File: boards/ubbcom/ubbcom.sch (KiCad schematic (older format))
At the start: 23 parts, among them U1 FT232RL

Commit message: blah, quick update... btw, this layout is horrible -- just testing to see if I can make this work
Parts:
- C1, C2, C3, R1, R2, R3: footprint (none) -> SM0805
- C4, FB1: footprint (none) -> SM0603
- D1, D2, D3: footprint (none) -> LED-1206
- PCTS1, PDCD1, PDCR1, PDTR1, PGND1, PRI1, PRTS1, PRXD1, PTXD1, PVCC1: footprint (none) -> SIL-1
- PUSB1: footprint (none) -> SIL-4
- U1: footprint (none) -> SSOP28
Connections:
- net GND: now also PUSB1.4 (P4); no longer PUSB1.1 (P1)
- net at PUSB1.2 (P2): now also U1.16 (USBD-); no longer U1.15 (USBD+)
- net at PUSB1.3 (P3): now also U1.15 (USBD+); no longer U1.16 (USBD-)
- net at C1.1, FB1.1: now also PUSB1.1 (P1); no longer PUSB1.4 (P4)
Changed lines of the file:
@@
-EESchema Schematic File Version 2  date Sun 13 May 2012 06:31:02 AM EDT
+EESchema Schematic File Version 2  date Sun 13 May 2012 07:41:58 AM EDT
 LIBS:power
 LIBS:device
@@
 F 0 "PUSB1" V 2000 2350 50  0000 C CNN
 F 1 "CONN_4" V 2100 2350 50  0000 C CNN
+F 2 "SIL-4" V 2200 2350 50  0001 C CNN
 	1    2050 2350
-	-1   0    0    1
+	-1   0    0    -1
 $EndComp
 $Comp
@@
 F 0 "FB1" H 2850 2350 60  0000 C CNN
 F 1 "FILTER" H 3100 2350 60  0000 C CNN
+F 2 "SM0603" H 3100 2450 60  0001 C CNN
 	1    3000 2200
 	1    0    0    -1
@@
 F 0 "C1" H 2600 2850 50  0000 L CNN
 F 1 "10nF" H 2600 2650 50  0000 L CNN
+F 2 "SM0805" H 2600 2750 50  0001 C CNN
 	1    2550 2750
 	1    0    0    -1
@@
 F 0 "C2" H 3500 2850 50  0000 L CNN
 F 1 "0.1uF" H 3350 2650 50  0000 L CNN
+F 2 "SM0805" H 3350 2750 50  0001 C CNN
 	1    3450 2750
 	1    0    0    -1
@@
 F 0 "C3" H 3800 2850 50  0000 L CNN
 F 1 "4.7uF" H 3650 2650 50  0000 L CNN
+F 2 "SM0805" H 3650 2750 50  0001 C CNN
 	1    3750 2750
 	1    0    0    -1
@@
 F 0 "D1" H 7000 3400 50  0000 C CNN
 F 1 "LED" H 7000 3200 50  0000 C CNN
+F 2 "LED-1206" H 7000 3300 50  0001 C CNN
 	1    7000 3300
 	0    -1   -1   0
@@
 F 0 "R1" V 7080 3800 50  0000 C CNN
 F 1 "1K" V 7000 3800 50  0000 C CNN
+F 2 "SM0805" V 7100 3800 50  0001 C CNN
 	1    7000 3800
 	1    0    0    -1
@@
 F 0 "U1" H 5250 3700 60  0000 C CNN
 F 1 "FT232RL" H 5650 1800 60  0000 L CNN
+F 2 "SSOP28" H 5650 1900 60  0001 C CNN
 	1    5250 2800
 	1    0    0    -1
@@
 F 0 "D2" H 6400 3400 50  0000 C CNN
 F 1 "LED" H 6400 3200 50  0000 C CNN
+F 2 "LED-1206" H 6400 3300 50  0001 C CNN
 	1    6400 3300
 	0    -1   -1   0
@@
 F 0 "D3" H 6700 3400 50  0000 C CNN
 F 1 "LED" H 6700 3200 50  0000 C CNN
+F 2 "LED-1206" H 6700 3300 50  0001 C CNN
 	1    6700 3300
 	0    -1   -1   0
@@
 F 0 "R3" V 6480 3800 50  0000 C CNN
 F 1 "1K" V 6400 3800 50  0000 C CNN
+F 2 "SM0805" V 6500 3800 50  0001 C CNN
 	1    6400 3800
 	1    0    0    -1
@@
 F 0 "R2" V 6780 3800 50  0000 C CNN
 F 1 "1K" V 6700 3800 50  0000 C CNN
+F 2 "SM0805" V 6800 3800 50  0001 C CNN
 	1    6700 3800
 	1    0    0    -1
@@
 F 0 "C4" H 4200 3600 50  0000 L CNN
 F 1 "0.1uF" H 4050 3400 50  0000 L CNN
+F 2 "SM0603" H 4050 3500 50  0001 C CNN
 	1    4150 3500
 	1    0    0    -1
@@
 F 0 "PTXD1" H 6630 2100 40  0000 L CNN
 F 1 "CONN_1" H 6550 2155 30  0001 C CNN
+F 2 "SIL-1" H 6550 2255 30  0001 C CNN
 	1    6550 2100
 	1    0    0    -1
@@
 F 0 "PRXD1" H 6630 2200 40  0000 L CNN
 F 1 "CONN_1" H 6550 2255 30  0001 C CNN
+F 2 "SIL-1" H 6550 2355 30  0001 C CNN
 	1    6550 2200
 	1    0    0    -1
@@
 F 0 "PRTS1" H 6630 2300 40  0000 L CNN
 F 1 "CONN_1" H 6550 2355 30  0001 C CNN
+F 2 "SIL-1" H 6550 2455 30  0001 C CNN
 	1    6550 2300
 	1    0    0    -1
@@
 F 0 "PCTS1" H 6630 2400 40  0000 L CNN
 F 1 "CONN_1" H 6550 2455 30  0001 C CNN
+F 2 "SIL-1" H 6550 2555 30  0001 C CNN
 	1    6550 2400
 	1    0    0    -1
@@
 F 0 "PDTR1" H 6630 2500 40  0000 L CNN
 F 1 "CONN_1" H 6550 2555 30  0001 C CNN
+F 2 "SIL-1" H 6550 2655 30  0001 C CNN
 	1    6550 2500
 	1    0    0    -1
@@
 F 0 "PDCR1" H 6630 2600 40  0000 L CNN
 F 1 "CONN_1" H 6550 2655 30  0001 C CNN
+F 2 "SIL-1" H 6550 2755 30  0001 C CNN
 	1    6550 2600
 	1    0    0    -1
@@
 F 0 "PDCD1" H 6630 2700 40  0000 L CNN
 F 1 "CONN_1" H 6550 2755 30  0001 C CNN
+F 2 "SIL-1" H 6550 2855 30  0001 C CNN
 	1    6550 2700
 	1    0    0    -1
@@
 F 0 "PRI1" H 6630 2800 40  0000 L CNN
 F 1 "CONN_1" H 6550 2855 30  0001 C CNN
+F 2 "SIL-1" H 6550 2955 30  0001 C CNN
 	1    6550 2800
 	1    0    0    -1
@@
 F 0 "PVCC1" H 7580 4050 40  0000 L CNN
 F 1 "CONN_1" H 7500 4105 30  0001 C CNN
+F 2 "SIL-1" H 7500 4205 30  0001 C CNN
 	1    7500 4050
 	1    0    0    -1
@@
 F 0 "PGND1" H 7580 3100 40  0000 L CNN
 F 1 "CONN_1" H 7500 3155 30  0001 C CNN
+F 2 "SIL-1" H 7500 3255 30  0001 C CNN
 	1    7500 3100
 	1    0    0    -1
 $EndComp
 Wire Wire Line
-	2400 2200 2550 2200
-Wire Wire Line
-	2550 2200 2650 2200
+	2400 2200 2650 2200
 Wire Wire Line
 	2400 2300 4300 2300
@@
 	4300 2150 4100 2150
 Wire Wire Line
-	4100 2050 4100 2150
-Wire Wire Line
-	4100 2150 4100 2200
+	4100 2050 4100 2200
 Connection ~ 4300 2150
 Wire Wire Line
-	4100 2200 3750 2200
-Wire Wire Line
-	3750 2200 3450 2200
-Wire Wire Line
-	3450 2200 3350 2200
+	4100 2200 3350 2200
 Connection ~ 4100 2150
 Wire Wire Line
@@
 	2400 2500 2400 2950
 Wire Wire Line
-	2400 2950 2550 2950
-Wire Wire Line
-	2550 2950 3000 2950
-Wire Wire Line
-	3000 2950 3450 2950
-Wire Wire Line
-	3450 2950 3750 2950
+	2400 2950 3750 2950
 Wire Wire Line
 	3450 2200 3450 2550
@@
 	6700 3500 6700 3550
 Wire Wire Line
-	6400 4050 6700 4050
-Wire Wire Line
-	6700 4050 7000 4050
-Wire Wire Line
-	7000 4050 7250 4050
-Wire Wire Line
-	7250 4050 7350 4050
+	6400 4050 7350 4050
 Wire Wire Line
 	7250 4050 7250 4000
@@
 	7000 3500 7000 3550
 Wire Wire Line
-	7000 3100 7250 3100
-Wire Wire Line
-	7250 3100 7350 3100
+	7000 3100 7350 3100
 Wire Wire Line
 	7250 3100 7250 3150
 Wire Wire Line
-	4950 4000 5100 4000
-Wire Wire Line
-	5100 4000 5250 4000
-Wire Wire Line
-	5250 4000 5400 4000
-Wire Wire Line
-	5400 4000 5550 4000
+	4950 4000 5550 4000
 Connection ~ 5100 4000
 Connection ~ 5100 4000

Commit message: yay done!
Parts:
- removed PDCD1, PDCR1, PRI1, PRTS1: CONN_1, SIL-1, symbol CONN_1
- added J1: USBPCB, SparkFun-USB-A-PCB, symbol USBPCB
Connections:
- net GND: now also J1.GND
- net at C1.1, FB1.1, PUSB1.1 (P1): now also J1.5V (VBUS)
- net at PUSB1.2 (P2), U1.16 (USBD-): now also J1.USBm (D-)
- net at PUSB1.3 (P3), U1.15 (USBD+): now also J1.USBp (D+)
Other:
- moved on the sheet: PUSB1
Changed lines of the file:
@@
-EESchema Schematic File Version 2  date Sun 13 May 2012 07:41:58 AM EDT
+EESchema Schematic File Version 2  date Tue 15 May 2012 01:46:11 AM EDT
 LIBS:power
 LIBS:device
@@
 LIBS:contrib
 LIBS:valves
-EELAYER 43  0
+LIBS:SparkFun
+LIBS:ubbcom-cache
+EELAYER 25  0
 EELAYER END
 $Descr A4 11693 8268
@@
 Sheet 1 1
 Title ""
-Date "13 may 2012"
+Date "15 may 2012"
 Rev ""
 Comp ""
@@
 L CONN_4 PUSB1
 U 1 1 4FAF7B95
-P 2050 2350
-F 0 "PUSB1" V 2000 2350 50  0000 C CNN
-F 1 "CONN_4" V 2100 2350 50  0000 C CNN
-F 2 "SIL-4" V 2200 2350 50  0001 C CNN
-	1    2050 2350
+P 1500 2350
+F 0 "PUSB1" V 1450 2350 50  0000 C CNN
+F 1 "CONN_4" V 1550 2350 50  0000 C CNN
+F 2 "SIL-4" V 1650 2350 50  0001 C CNN
+	1    1500 2350
 	-1   0    0    -1
 $EndComp
@@
 $EndComp
 $Comp
-L CONN_1 PRTS1
-U 1 1 4FAF87D2
-P 6550 2300
-F 0 "PRTS1" H 6630 2300 40  0000 L CNN
-F 1 "CONN_1" H 6550 2355 30  0001 C CNN
-F 2 "SIL-1" H 6550 2455 30  0001 C CNN
-	1    6550 2300
-	1    0    0    -1
-$EndComp
-$Comp
 L CONN_1 PCTS1
 U 1 1 4FAF87D9
@@
 $EndComp
 $Comp
-L CONN_1 PDCR1
-U 1 1 4FAF87E7
-P 6550 2600
-F 0 "PDCR1" H 6630 2600 40  0000 L CNN
-F 1 "CONN_1" H 6550 2655 30  0001 C CNN
-F 2 "SIL-1" H 6550 2755 30  0001 C CNN
-	1    6550 2600
-	1    0    0    -1
-$EndComp
-$Comp
-L CONN_1 PDCD1
-U 1 1 4FAF87EE
-P 6550 2700
-F 0 "PDCD1" H 6630 2700 40  0000 L CNN
-F 1 "CONN_1" H 6550 2755 30  0001 C CNN
-F 2 "SIL-1" H 6550 2855 30  0001 C CNN
-	1    6550 2700
-	1    0    0    -1
-$EndComp
-$Comp
-L CONN_1 PRI1
-U 1 1 4FAF87F5
-P 6550 2800
-F 0 "PRI1" H 6630 2800 40  0000 L CNN
-F 1 "CONN_1" H 6550 2855 30  0001 C CNN
-F 2 "SIL-1" H 6550 2955 30  0001 C CNN
-	1    6550 2800
-	1    0    0    -1
-$EndComp
-$Comp
 L CONN_1 PVCC1
 U 1 1 4FAF8880
@@
 	1    0    0    -1
 $EndComp
-Wire Wire Line
-	2400 2200 2650 2200
-Wire Wire Line
-	2400 2300 4300 2300
+$Comp
+L USBPCB J1
+U 1 1 4FB1EF10
+P 1950 2000
+F 0 "J1" H 2050 2400 50  0000 C CNN
+F 1 "USBPCB" H 2050 1900 50  0000 C CNN
+F 2 "SparkFun-USB-A-PCB" H 2050 1800 50  0001 C CNN
+	1    1950 2000
+	0    1    -1   0
+$EndComp
+Wire Wire Line
+	2650 2200 1850 2200
+Wire Wire Line
+	1850 2300 4300 2300
 Wire Wire Line
 	4300 2300 4300 2400
 Wire Wire Line
-	2400 2400 4200 2400
+	1850 2400 4200 2400
 Wire Wire Line
 	4200 2400 4200 2500
@@
 Connection ~ 2550 2200
 Wire Wire Line
-	2400 2500 2400 2950
+	2400 2950 2400 2500
 Wire Wire Line
 	2400 2950 3750 2950
@@
 Connection ~ 3000 2950
 Wire Wire Line
-	6150 2300 6400 2300
-Wire Wire Line
 	6150 2400 6400 2400
 Wire Wire Line
 	6150 2500 6400 2500
-Wire Wire Line
-	6150 2600 6400 2600
-Wire Wire Line
-	6150 2700 6400 2700
-Wire Wire Line
-	6150 2800 6400 2800
 Connection ~ 7250 4050
 Connection ~ 7250 4050
 Connection ~ 7250 3100
 Connection ~ 7250 3100
+Wire Wire Line
+	2050 2200 2050 2100
+Wire Wire Line
+	2150 2300 2150 2100
+Wire Wire Line
+	2250 2400 2250 2100
+Wire Wire Line
+	1950 2100 1950 2500
+Wire Wire Line
+	2400 2500 1850 2500
+Connection ~ 2050 2200
+Connection ~ 2150 2300
+Connection ~ 2250 2400
+Connection ~ 1950 2500
 $EndSCHEMATC

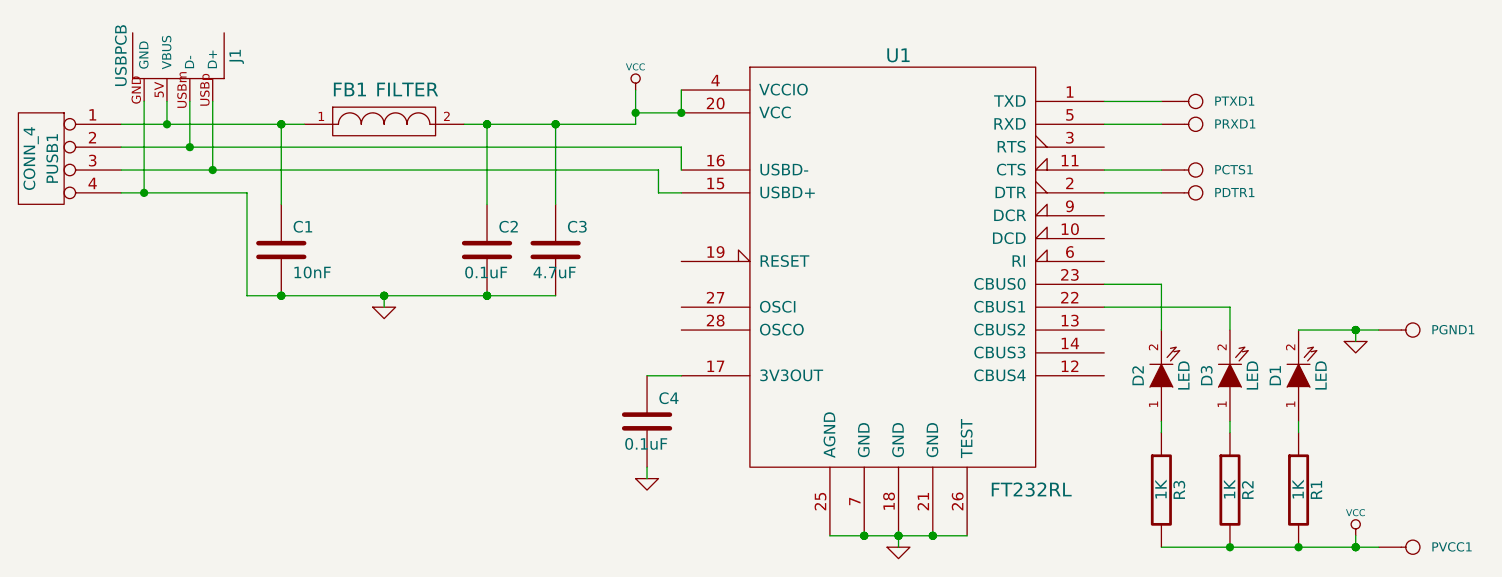
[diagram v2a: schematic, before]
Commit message: update to include txden and rts
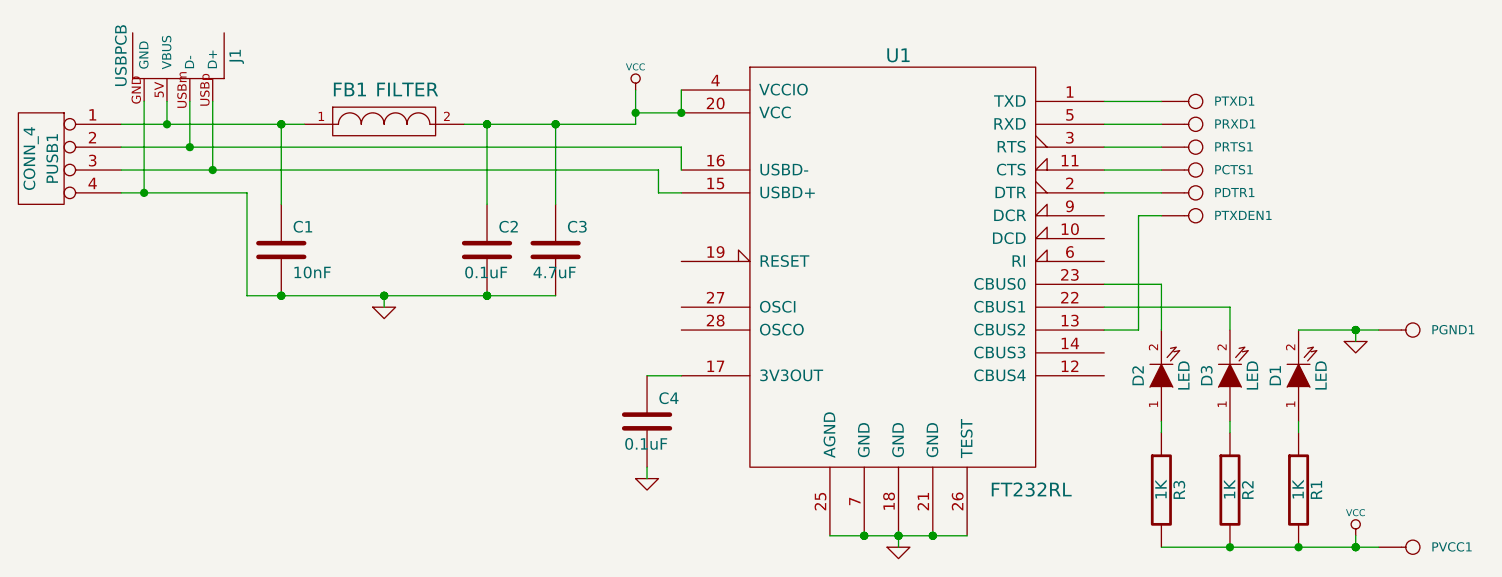
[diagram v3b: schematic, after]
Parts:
- added PRTS1, PTXDEN1: CONN_1, SIL-1, symbol CONN_1
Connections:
- net at U1.13 (CBUS2): now also PTXDEN1.1
- net at U1.3 (RTS): now also PRTS1.1
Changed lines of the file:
@@
-EESchema Schematic File Version 2  date Tue 15 May 2012 01:46:11 AM EDT
+EESchema Schematic File Version 2  date Sun 01 Jul 2012 02:29:22 PM EDT
 LIBS:power
 LIBS:device
@@
 Sheet 1 1
 Title ""
-Date "15 may 2012"
+Date "1 jul 2012"
 Rev ""
 Comp ""
@@
 F 2 "SIL-1" H 6550 2655 30  0001 C CNN
 	1    6550 2500
-	1    0    0    -1
+	1    0    0    1
 $EndComp
 $Comp
@@
 	0    1    -1   0
 $EndComp
+$Comp
+L CONN_1 PRTS1
+U 1 1 4FF08721
+P 6550 2300
+F 0 "PRTS1" H 6630 2300 40  0000 L CNN
+F 1 "CONN_1" H 6550 2355 30  0001 C CNN
+F 2 "SIL-1" H 6550 2455 30  0001 C CNN
+	1    6550 2300
+	1    0    0    -1
+$EndComp
+$Comp
+L CONN_1 PTXDEN1
+U 1 1 4FF088B4
+P 6550 2600
+F 0 "PTXDEN1" H 6630 2600 40  0000 L CNN
+F 1 "CONN_1" H 6550 2655 30  0001 C CNN
+F 2 "SIL-1" H 6550 2755 30  0001 C CNN
+	1    6550 2600
+	1    0    0    1
+$EndComp
 Wire Wire Line
 	2650 2200 1850 2200
@@
 	4300 2150 4100 2150
 Wire Wire Line
-	4100 2050 4100 2200
+	4100 2200 4100 2050
 Connection ~ 4300 2150
 Wire Wire Line
-	4100 2200 3350 2200
+	3350 2200 4100 2200
 Connection ~ 4100 2150
 Wire Wire Line
@@
 Connection ~ 2550 2200
 Wire Wire Line
-	2400 2950 2400 2500
-Wire Wire Line
-	2400 2950 3750 2950
+	2400 2500 2400 2950
+Wire Wire Line
+	3750 2950 2400 2950
 Wire Wire Line
 	3450 2200 3450 2550
@@
 	1950 2100 1950 2500
 Wire Wire Line
-	2400 2500 1850 2500
+	1850 2500 2400 2500
 Connection ~ 2050 2200
 Connection ~ 2150 2300
 Connection ~ 2250 2400
 Connection ~ 1950 2500
+Wire Wire Line
+	6150 2300 6400 2300
+Wire Wire Line
+	6150 3100 6300 3100
+Wire Wire Line
+	6300 3100 6300 2600
+Wire Wire Line
+	6300 2600 6400 2600
 $EndSCHEMATC

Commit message: redesigned to use a real USB connector instead of a PCB one (hint: they don't work)
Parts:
- J1: footprint SparkFun-USB-A-PCB -> USB-A-SMD; Part (none) -> 1001-011-01101; URL (none) -> http://www.digikey.com/scripts/DkSearch/dksus.dll?wt.z_head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
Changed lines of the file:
@@
-EESchema Schematic File Version 2  date Sun 01 Jul 2012 02:29:22 PM EDT
+EESchema Schematic File Version 2  date Fri 06 Jul 2012 05:03:35 AM EDT
 LIBS:power
 LIBS:device
@@
 Sheet 1 1
 Title ""
-Date "1 jul 2012"
+Date "6 jul 2012"
 Rev ""
 Comp ""
@@
 F 0 "J1" H 2050 2400 50  0000 C CNN
 F 1 "USBPCB" H 2050 1900 50  0000 C CNN
-F 2 "SparkFun-USB-A-PCB" H 2050 1800 50  0001 C CNN
+F 2 "USB-A-SMD" H 2050 1800 50  0001 C CNN
+F 4 "1001-011-01101" H 1950 2000 60  0001 C CNN "Part"
+F 5 "http://www.digikey.com/scripts/DkSearch/dksus.dll?wt.z_header=search_go&lang=en&keywords=1175-1008-nd&cur=USD" H 1950 2000 60  0001 C CNN "URL"
 	1    1950 2000
 	0    1    -1   0
